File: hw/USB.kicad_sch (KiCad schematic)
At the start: 4 parts, among them J3 USB_C_Receptacle_USB2.0, U3 PUSB3FR4

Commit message: updated sheets information
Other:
- company: (none) -> Qingdao IotPi Information Technology Ltd.,
- title: (none) -> KiCad 2023 Shen Zhen Badge
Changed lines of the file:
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@@
 (kicad_sch (version 20230121) (generator eeschema)
   (paper "A4")
+  (title_block
+    (title "KiCad 2023 Shen Zhen Badge")
+    (date "2023-09-04")
+    (rev "1")
+    (company "Qingdao IotPi Information Technology Ltd.,")
+    (comment 1 "Designed by Yang Hongbo")
+  )
   (junction (at 71.12 66.04) (diameter 0) (color 0 0 0 0)
   )

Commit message: updated Designs
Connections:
- net USB_DN: now also U3.4 (CH3); no longer U3.1 (CH1)
- net USB_DP: now also U3.5 (CH4); no longer U3.2 (CH2)
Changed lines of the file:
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@@
   (junction (at 48.26 106.68) (diameter 0) (color 0 0 0 0)
   )
-  (no_connect (at 138.43 120.65))
+  (no_connect (at 130.81 120.65))
   (no_connect (at 63.5 93.98))
-  (no_connect (at 135.89 120.65))
+  (no_connect (at 128.27 120.65))
   (no_connect (at 63.5 96.52))
   (wire (pts (xy 193.04 73.66) (xy 180.34 73.66))
@@
     (stroke (width 0) (type default))
   )
-  (wire (pts (xy 130.81 120.65) (xy 130.81 107.95))
+  (wire (pts (xy 138.43 120.65) (xy 138.43 107.95))
     (stroke (width 0) (type default))
   )
@@
     (stroke (width 0) (type default))
   )
-  (wire (pts (xy 128.27 120.65) (xy 128.27 107.95))
+  (wire (pts (xy 135.89 120.65) (xy 135.89 107.95))
     (stroke (width 0) (type default))
   )
@@
     (effects (font (size 1.27 1.27)) (justify left bottom))
   )
-  (label "USB_DN" (at 128.27 107.95 90) (fields_autoplaced)
+  (label "USB_DN" (at 135.89 107.95 90) (fields_autoplaced)
     (effects (font (size 1.27 1.27)) (justify left bottom))
   )
@@
     (effects (font (size 1.27 1.27)) (justify right bottom))
   )
-  (label "USB_DP" (at 130.81 107.95 90) (fields_autoplaced)
+  (label "USB_DP" (at 138.43 107.95 90) (fields_autoplaced)
     (effects (font (size 1.27 1.27)) (justify left bottom))
   )

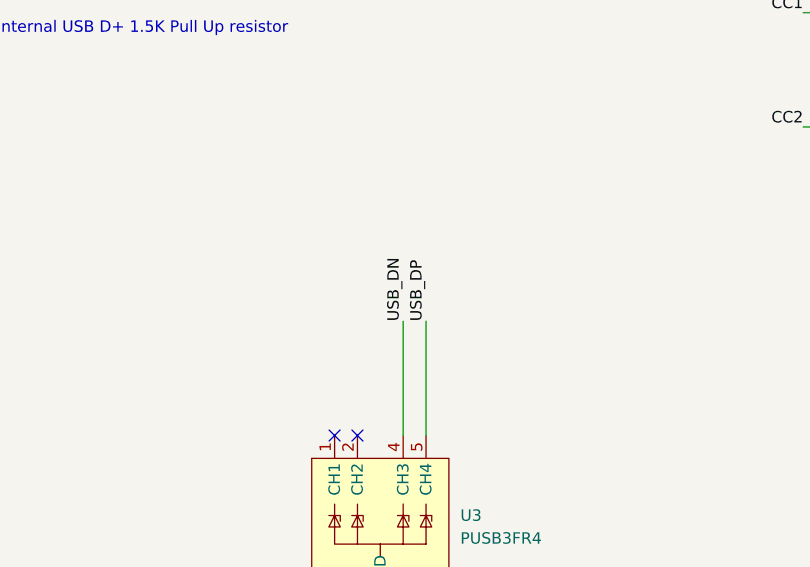
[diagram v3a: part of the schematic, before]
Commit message: routed USB
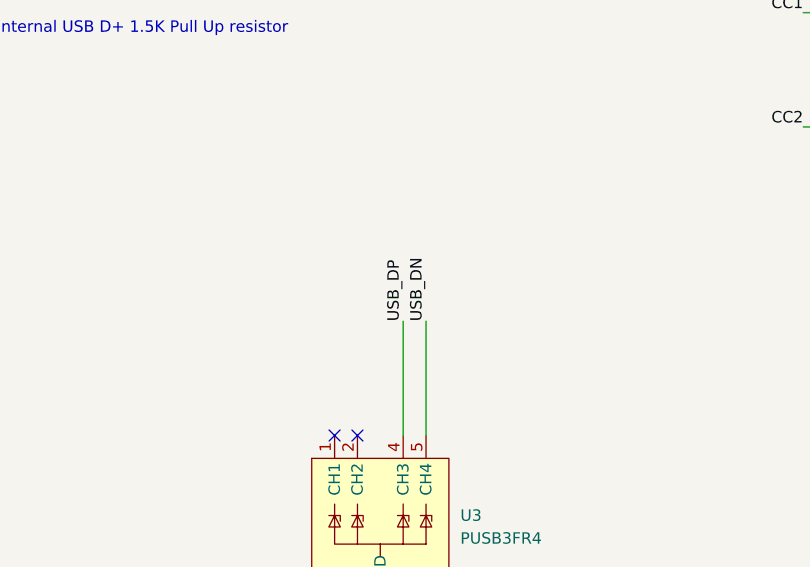
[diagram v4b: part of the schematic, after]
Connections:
- net USB_DN: now also U3.5 (CH4); no longer U3.4 (CH3)
- net USB_DP: now also U3.4 (CH3); no longer U3.5 (CH4)
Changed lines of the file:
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@@
     (stroke (width 0) (type default))
   )
-  (wire (pts (xy 138.43 120.65) (xy 138.43 107.95))
+  (wire (pts (xy 135.89 120.65) (xy 135.89 107.95))
     (stroke (width 0) (type default))
   )
@@
     (stroke (width 0) (type default))
   )
-  (wire (pts (xy 135.89 120.65) (xy 135.89 107.95))
+  (wire (pts (xy 138.43 120.65) (xy 138.43 107.95))
     (stroke (width 0) (type default))
   )
@@
     (effects (font (size 1.27 1.27)) (justify left bottom))
   )
-  (label "USB_DN" (at 135.89 107.95 90) (fields_autoplaced)
+  (label "USB_DN" (at 138.43 107.95 90) (fields_autoplaced)
     (effects (font (size 1.27 1.27)) (justify left bottom))
   )
@@
     (effects (font (size 1.27 1.27)) (justify right bottom))
   )
-  (label "USB_DP" (at 138.43 107.95 90) (fields_autoplaced)
+  (label "USB_DP" (at 135.89 107.95 90) (fields_autoplaced)
     (effects (font (size 1.27 1.27)) (justify left bottom))
   )
